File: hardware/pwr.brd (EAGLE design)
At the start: 45 x 28 mm, 21 parts, among them IC2 LM2675M-ADJ, Q2 IRFR5305, T1 BC846, T2 BC846, X3 MKDSN1,5/4-5,08

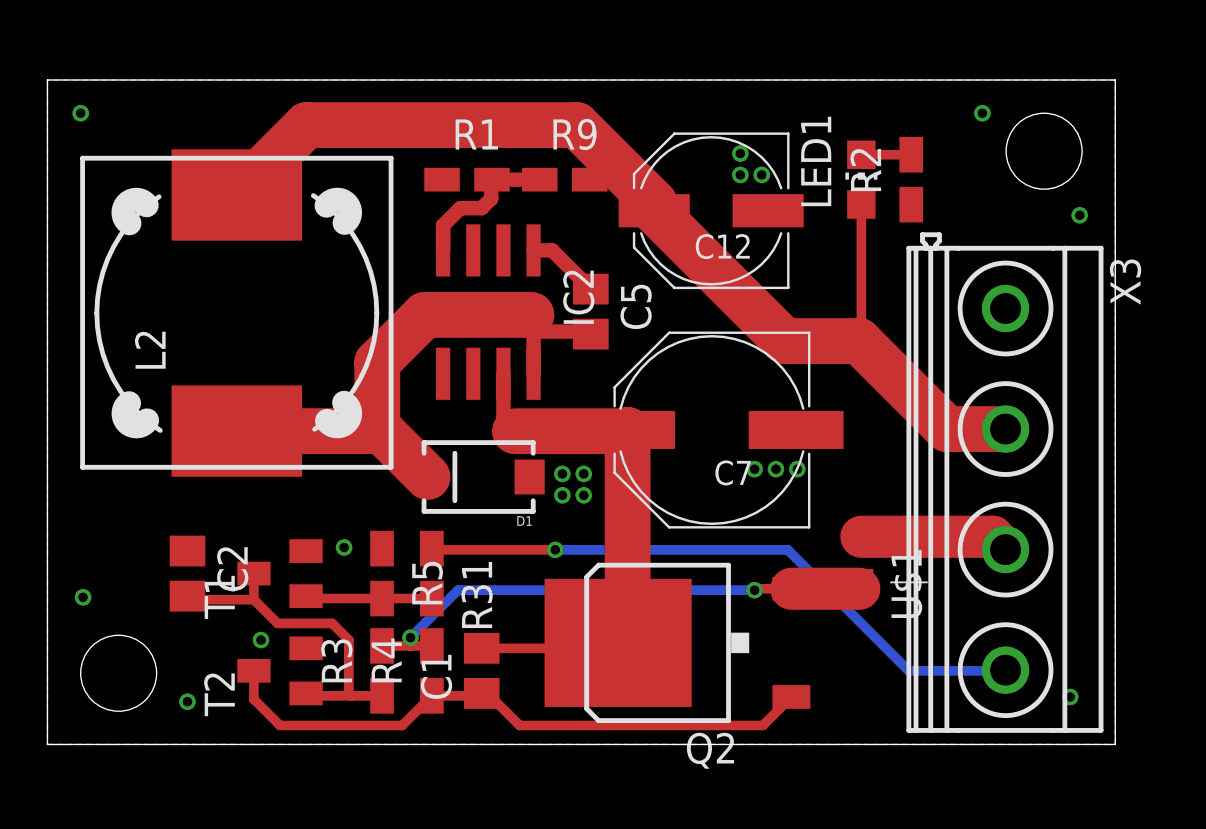
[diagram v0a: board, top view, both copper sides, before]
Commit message: pwr board  width decrease
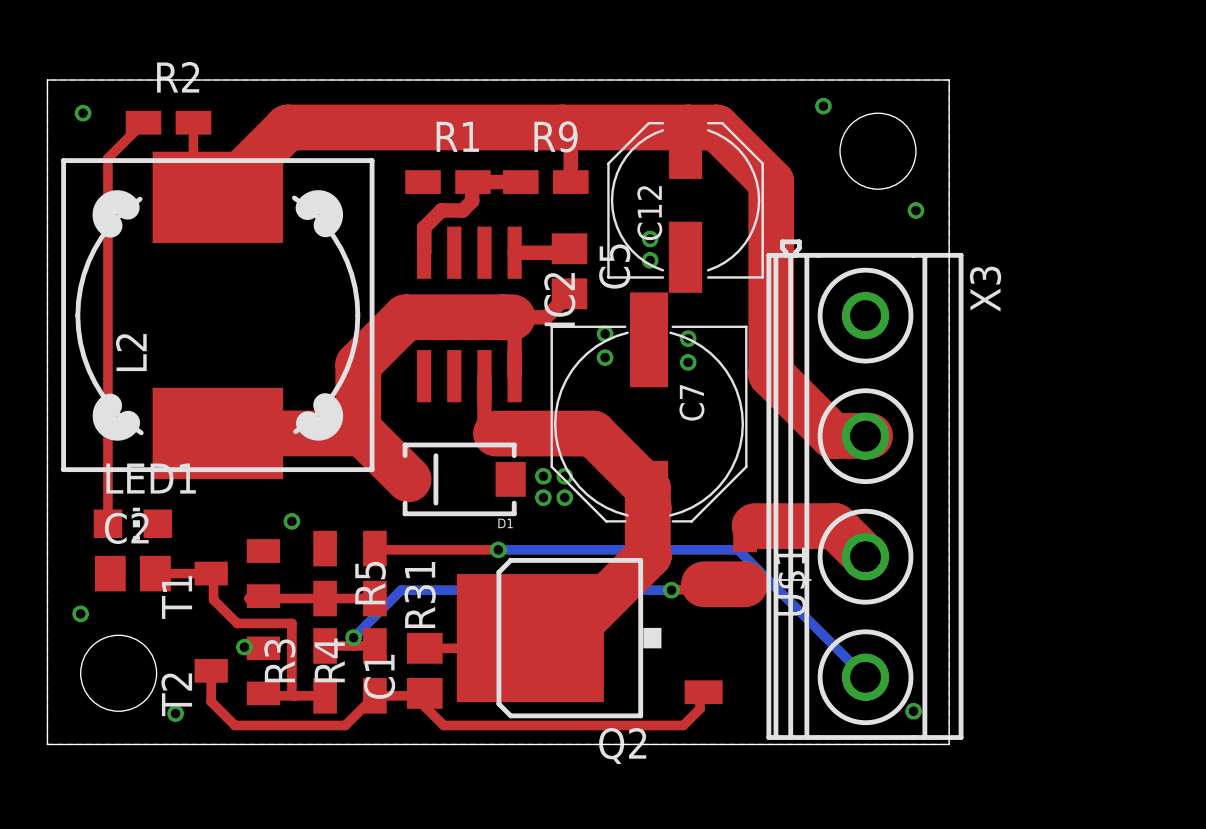
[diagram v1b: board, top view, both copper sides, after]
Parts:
- moved LED1 34.0 mm to (3.60, 9.30), turned to 270 degrees
- moved R2 31.4 mm to (5.10, 26.2), turned to 0 degrees
- moved X3 5.91 mm to (34.5, 10.4)
- moved U$1 4.90 mm to (29.4, 7.80)
- moved Q2 3.71 mm to (22.9, 4.48)
- moved C7 2.66 mm to (25.4, 13.5), turned to 270 degrees
- moved C1 2.40 mm to (15.9, 3.10)
- moved R3 2.40 mm to (11.7, 3.10)
- moved R5 2.40 mm to (11.7, 7.20)
- moved R31 2.40 mm to (13.8, 7.20)
- moved R4 2.40 mm to (13.8, 3.10)
- moved C2 2.30 mm to (3.60, 7.20), turned to 0 degrees
- moved C5 1.92 mm to (22.0, 19.9)
- moved T1 1.80 mm to (8.00, 7.20)
- moved T2 1.80 mm to (8.00, 3.10)
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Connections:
- net GND: now also LED1.C; no longer R2.1
- net N$1: now also LED1.A, R2.1; no longer LED1.C, R2.2
- net V_OUT: now also R2.2; no longer LED1.A
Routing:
- net N$1: track 2.10 -> 17.5 mm
- net CE: track 26.3 -> 22.9 mm
- net N$49: track 24.7 -> 28.1 mm
- net N$5: track 22.3 -> 19.9 mm
- net GND: track 0.00 -> 0.82 mm
- net N$9: track 24.1 -> 24.8 mm
- net N$16: track 25.9 -> 25.2 mm
- net N$10: track 3.09 -> 2.39 mm
- net V_IN: track 6.30 -> 5.75 mm
- net N$3: track 5.70 -> 6.21 mm
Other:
- board size 45 x 28 mm -> 38 x 28 mm

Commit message: pwr board width decrease
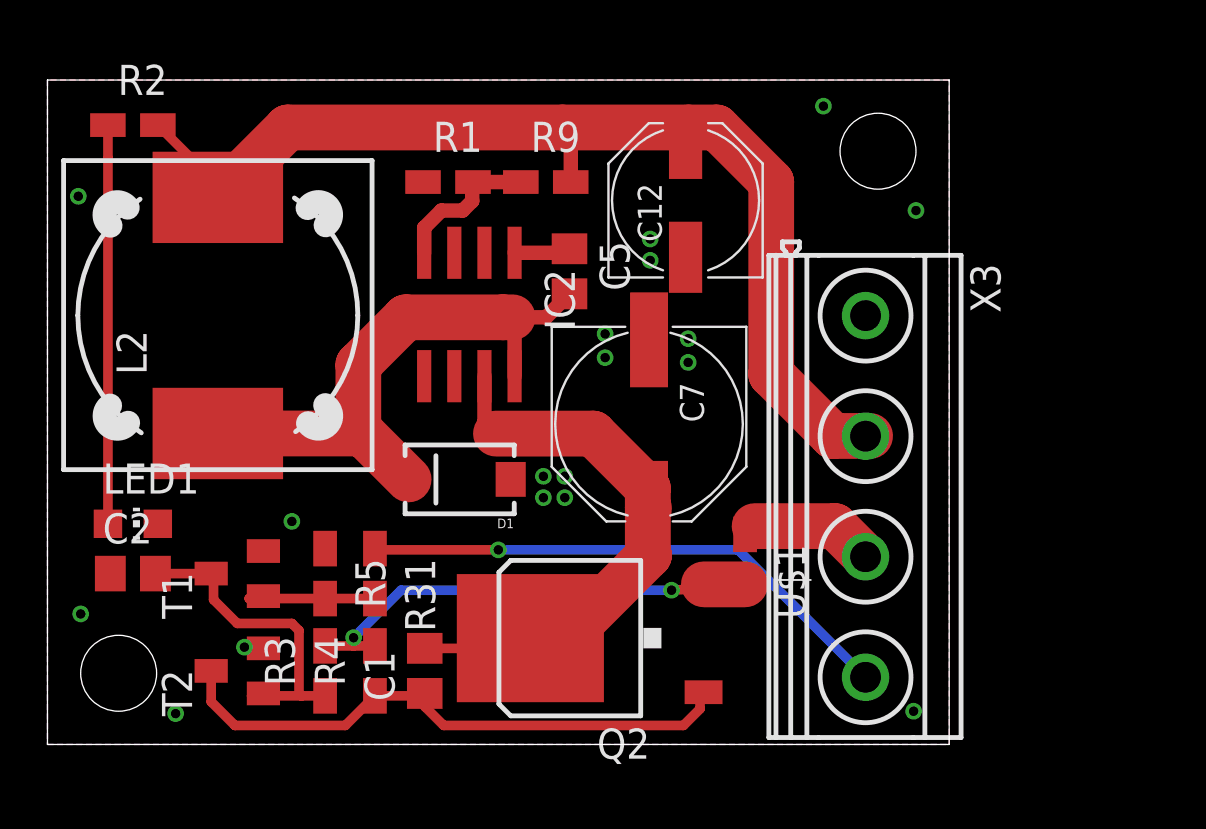
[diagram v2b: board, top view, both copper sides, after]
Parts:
- moved R2 1.50 mm to (3.60, 26.1)
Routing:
- net V_OUT: track 46.1 -> 46.9 mm
- net N$1: track 17.5 -> 16.8 mm
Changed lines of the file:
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@@
 </element>
 <element name="LED1" library="led" package="CHIP-LED0805" value="status" x="3.6" y="9.3" rot="R270"/>
-<element name="R2" library="rcl" package="R0805W" value="200k" x="5.1" y="26.2"/>
+<element name="R2" library="rcl" package="R0805W" value="200k" x="3.6" y="26.1"/>
 <element name="U$1" library="Simplex-Fuses" package="0805W" value="RESETTABLE_0805" x="29.4" y="7.8" rot="R270"/>
 <element name="T1" library="transistor" package="SOT23" value="BC846" x="8" y="7.2" rot="R90"/>
@@
 <via x="10.3" y="9.4" extent="1-16" drill="0.4"/>
 <via x="8.3" y="4.1" extent="1-16" drill="0.4"/>
-<via x="1.5" y="26.6" extent="1-16" drill="0.4"/>
+<via x="1.3" y="23.1" extent="1-16" drill="0.4"/>
 <via x="1.4" y="5.5" extent="1-16" drill="0.4"/>
 <via x="5.4" y="1.3" extent="1-16" drill="0.4"/>
@@
 <wire x1="27.29" y1="25.71" x2="27" y2="26" width="0.6096" layer="1"/>
 <contactref element="R2" pad="2"/>
-<wire x1="6.1525" y1="26.2" x2="6.1525" y2="23.5475" width="0.4064" layer="1"/>
-<wire x1="6.1525" y1="23.5475" x2="6.6" y2="23.1" width="0.4064" layer="1"/>
+<wire x1="6.1525" y1="23.5475" x2="6.3" y2="23.4" width="0.4064" layer="1"/>
+<wire x1="6.3" y1="23.4" x2="6.6" y2="23.1" width="0.4064" layer="1"/>
 <wire x1="6.6" y1="23.1" x2="7.135" y2="23.1" width="0.4064" layer="1"/>
 <wire x1="7.135" y1="23.1" x2="7.18" y2="23.055" width="0.4064" layer="1"/>
@@
 <wire x1="33.1" y1="13" x2="34.4661" y2="13" width="1.9304" layer="1"/>
 <wire x1="34.4661" y1="13" x2="34.475" y2="12.9911" width="1.9304" layer="1"/>
+<wire x1="4.6525" y1="26.1" x2="6.3" y2="24.4525" width="0.4064" layer="1"/>
+<wire x1="6.3" y1="24.4525" x2="6.3" y2="23.4" width="0.4064" layer="1"/>
 </signal>
 <signal name="N$2">
@@
 <contactref element="R3" pad="1"/>
 <wire x1="9.1" y1="2.15" x2="8.6025" y2="2.0475" width="0.4064" layer="1"/>
-<wire x1="8.6025" y1="2.0475" x2="10.4" y2="2.0475" width="0.4064" layer="1"/>
-<wire x1="10.4" y1="2.0475" x2="11.7" y2="2.0475" width="0.4064" layer="1"/>
-<wire x1="10.3" y1="5.1" x2="10.3" y2="2.1475" width="0.4064" layer="1"/>
-<wire x1="10.3" y1="2.1475" x2="10.4" y2="2.0475" width="0.4064" layer="1"/>
+<wire x1="8.6025" y1="2.0475" x2="10.7" y2="2.0475" width="0.4064" layer="1"/>
 <contactref element="C2" pad="2"/>
+<wire x1="10.7" y1="2.0475" x2="11.7" y2="2.0475" width="0.4064" layer="1"/>
 <wire x1="4.55" y1="7.2" x2="6.9" y2="7.2" width="0.4064" layer="1"/>
-<wire x1="10.3" y1="5.1" x2="8" y2="5.1" width="0.4064" layer="1"/>
 <wire x1="8" y1="5.1" x2="7" y2="6.1" width="0.4064" layer="1"/>
 <wire x1="7" y1="6.1" x2="7" y2="7.1" width="0.4064" layer="1"/>
 <wire x1="7" y1="7.1" x2="6.9" y2="7.2" width="0.4064" layer="1"/>
+<wire x1="8" y1="5.1" x2="10.3" y2="5.1" width="0.4064" layer="1"/>
+<wire x1="10.3" y1="5.1" x2="10.6" y2="4.8" width="0.4064" layer="1"/>
+<wire x1="10.6" y1="4.8" x2="10.6" y2="2.1475" width="0.4064" layer="1"/>
+<wire x1="10.6" y1="2.1475" x2="10.7" y2="2.0475" width="0.4064" layer="1"/>
 </signal>
 <signal name="N$3">
@@
 <contactref element="R2" pad="1"/>
 <wire x1="2.55" y1="9.3" x2="2.55" y2="24.7025" width="0.4064" layer="1"/>
-<wire x1="2.55" y1="24.7025" x2="4.0475" y2="26.2" width="0.4064" layer="1"/>
+<wire x1="2.55" y1="24.7025" x2="2.5475" y2="26.1" width="0.4064" layer="1"/>
 </signal>
 </signals>

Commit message: board ready
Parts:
- removed C1: 10nF, rcl:C0805
- removed IC2: LM2675M-ADJ, Simplex-ICs:SO-08
- removed Q2: IRFR5305, transistor-power:D-PAK_TO252AA
- removed R4: 220k, rcl:R0805W
- removed R9: 4.75k 1%, rcl:R0805W
- removed T2: BC846, transistor:SOT23
- added IC1: (no value), Simplex-ICs:SO-08
- added R10: 200k, rcl:R0805W
- R2: value 200k -> 4k
- moved R2 22.3 mm to (19.5, 10.4), turned to 270 degrees
- moved U$1 16.4 mm to (31.3, 24.1), turned to 90 degrees
- moved R1 14.1 mm to (21.6, 10.4), turned to 90 degrees
- moved LED1 13.6 mm to (17.2, 10.4), turned to 180 degrees
- moved C12 12.8 mm to (26.1, 10.2), turned to 270 degrees
- moved D1 12.3 mm to (18.8, 23.4)
- moved T1 11.5 mm to (18.7, 3.10), turned to 180 degrees
- moved R5 10.9 mm to (21.8, 3.10)
- moved R31 10.9 mm to (23.9, 3.10)
- moved C2 10.6 mm to (13.4, 3.10), turned to 270 degrees
- moved C7 7.63 mm to (26.1, 21.1), turned to 90 degrees
- moved C5 7.04 mm to (15.0, 19.2), turned to 90 degrees
- moved R3 3.90 mm to (15.6, 3.10)
- moved L2 0.68 mm to (7.02, 17.4), turned to 270 degrees
- moved X3 0.20 mm to (34.5, 10.6)
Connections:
- removed net N$16: C1.1, Q2.1, R4.1, T2.3
- removed net N$5: Q2.3, R3.2, R4.2, U$1.2
- net CE: now also X3.3; no longer X3.4
- net GND: now also IC1.2, IC1.3, IC1.6, X3.4; no longer IC2.6, T2.2, X3.1
- net N$1: now also R10.1; no longer R2.1
- net N$10: now also IC1.1; no longer IC2.1
- net N$2: now also IC1.5; no longer T2.1
- net N$4: now also IC1.4, R2.1; no longer IC2.4, R9.1
- net N$49: now also IC1.7, R3.2, U$1.2; no longer C1.2, IC2.7, Q2.4
- net N$9: now also IC1.8; no longer IC2.8
- net V_IN: now also X3.1; no longer X3.3
- net V_OUT: now also R10.2; no longer R9.2
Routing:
- net N$16: track 25.2 -> 0.00 mm
- net N$5: track 19.9 -> 0.00 mm, vias 2 -> 0
- net N$1: track 16.8 -> 2.30 mm
- net N$2: track 14.0 -> 26.6 mm, vias 0 -> 2
- net CE: track 22.9 -> 12.2 mm, vias 1 -> 0
- net N$49: track 28.1 -> 37.6 mm, vias 0 -> 2
- net V_OUT: track 46.9 -> 39.5 mm
- net N$9: track 24.8 -> 19.0 mm
- net N$10: track 2.39 -> 4.76 mm
- net N$4: track 6.37 -> 5.58 mm
- net GND: track 0.82 -> 1.02 mm, vias 18 -> 16
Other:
- board text added: "R1"
- board text added: "R2"
- board text added: "V_IN = 6.5 - 40V V_OUT = 1.21(1+R2/R1)"
- board text added: "V_IN V_OUT CE GND"
